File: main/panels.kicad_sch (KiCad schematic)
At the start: 1 part, among them U1 Adafruit 2717

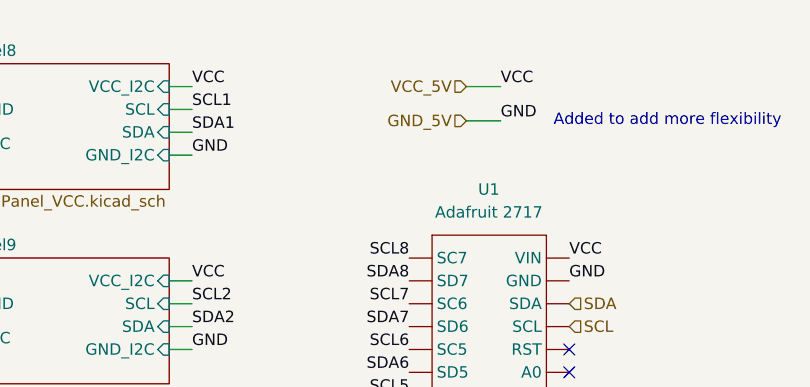
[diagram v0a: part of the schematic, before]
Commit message: added MCU to PV
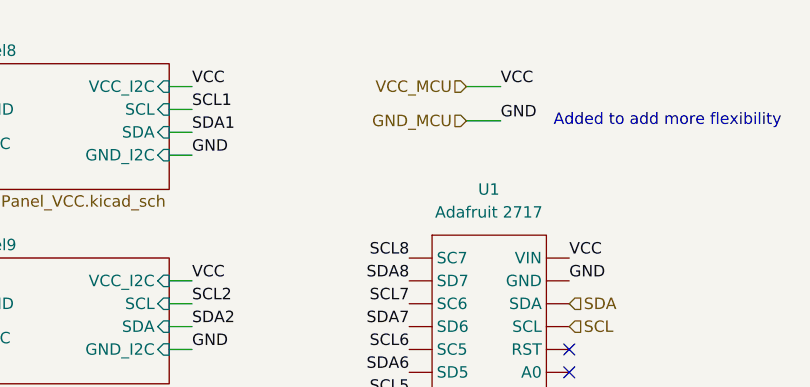
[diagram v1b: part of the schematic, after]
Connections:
- net GND_5V is gone; now on net VCC_MCU: U1. (VIN)
- net VCC_5V is gone; now on net VCC_MCU: U1. (VIN)
- net VCC_MCU: now reaches U1. (VIN)
- new net GND_MCU: U1. (VIN)
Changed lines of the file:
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@@
 		)
 	)
-	(hierarchical_label "GND_5V"
+	(hierarchical_label "GND_MCU"
 		(shape input)
 		(at 133.35 27.94 180)
@@
 		)
 	)
-	(hierarchical_label "VCC_5V"
+	(hierarchical_label "VCC_MCU"
 		(shape input)
 		(at 133.35 24.13 180)

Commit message: added logos, oranised sheets, final version
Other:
- company: (none) -> Designers: Krzysztof Grajek, Wojtek Kołodziej
- title: (none) -> Panels schematic
